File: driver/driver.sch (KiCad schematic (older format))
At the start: 103 parts, among them J1 OUT_A, J10 FAN, J2 OUT_B, J4 RJ45_LED_Shielded, J5 RJ45_LED_Shielded, J6 1602 I2C LCD, J7 IN_VCC, J8 IN_GND, J9 SWD, Q1 TPHR6503PL, Q2 TPHR6503PL, Q3 TPHR6503PL, Q4 TPHR6503PL, U1 MT3608, U10 PC817, U11 AMS1117-5.0, U12 PC817, U13 MAX485E, U2 74HC595, U3 AMS1117-3.3, U4 TC4427, U5 TC4427, U6 STM32F030F4Px, U7 INA226, U8 MCP9804_MSOP, U9 PC817, Y1 8MHz

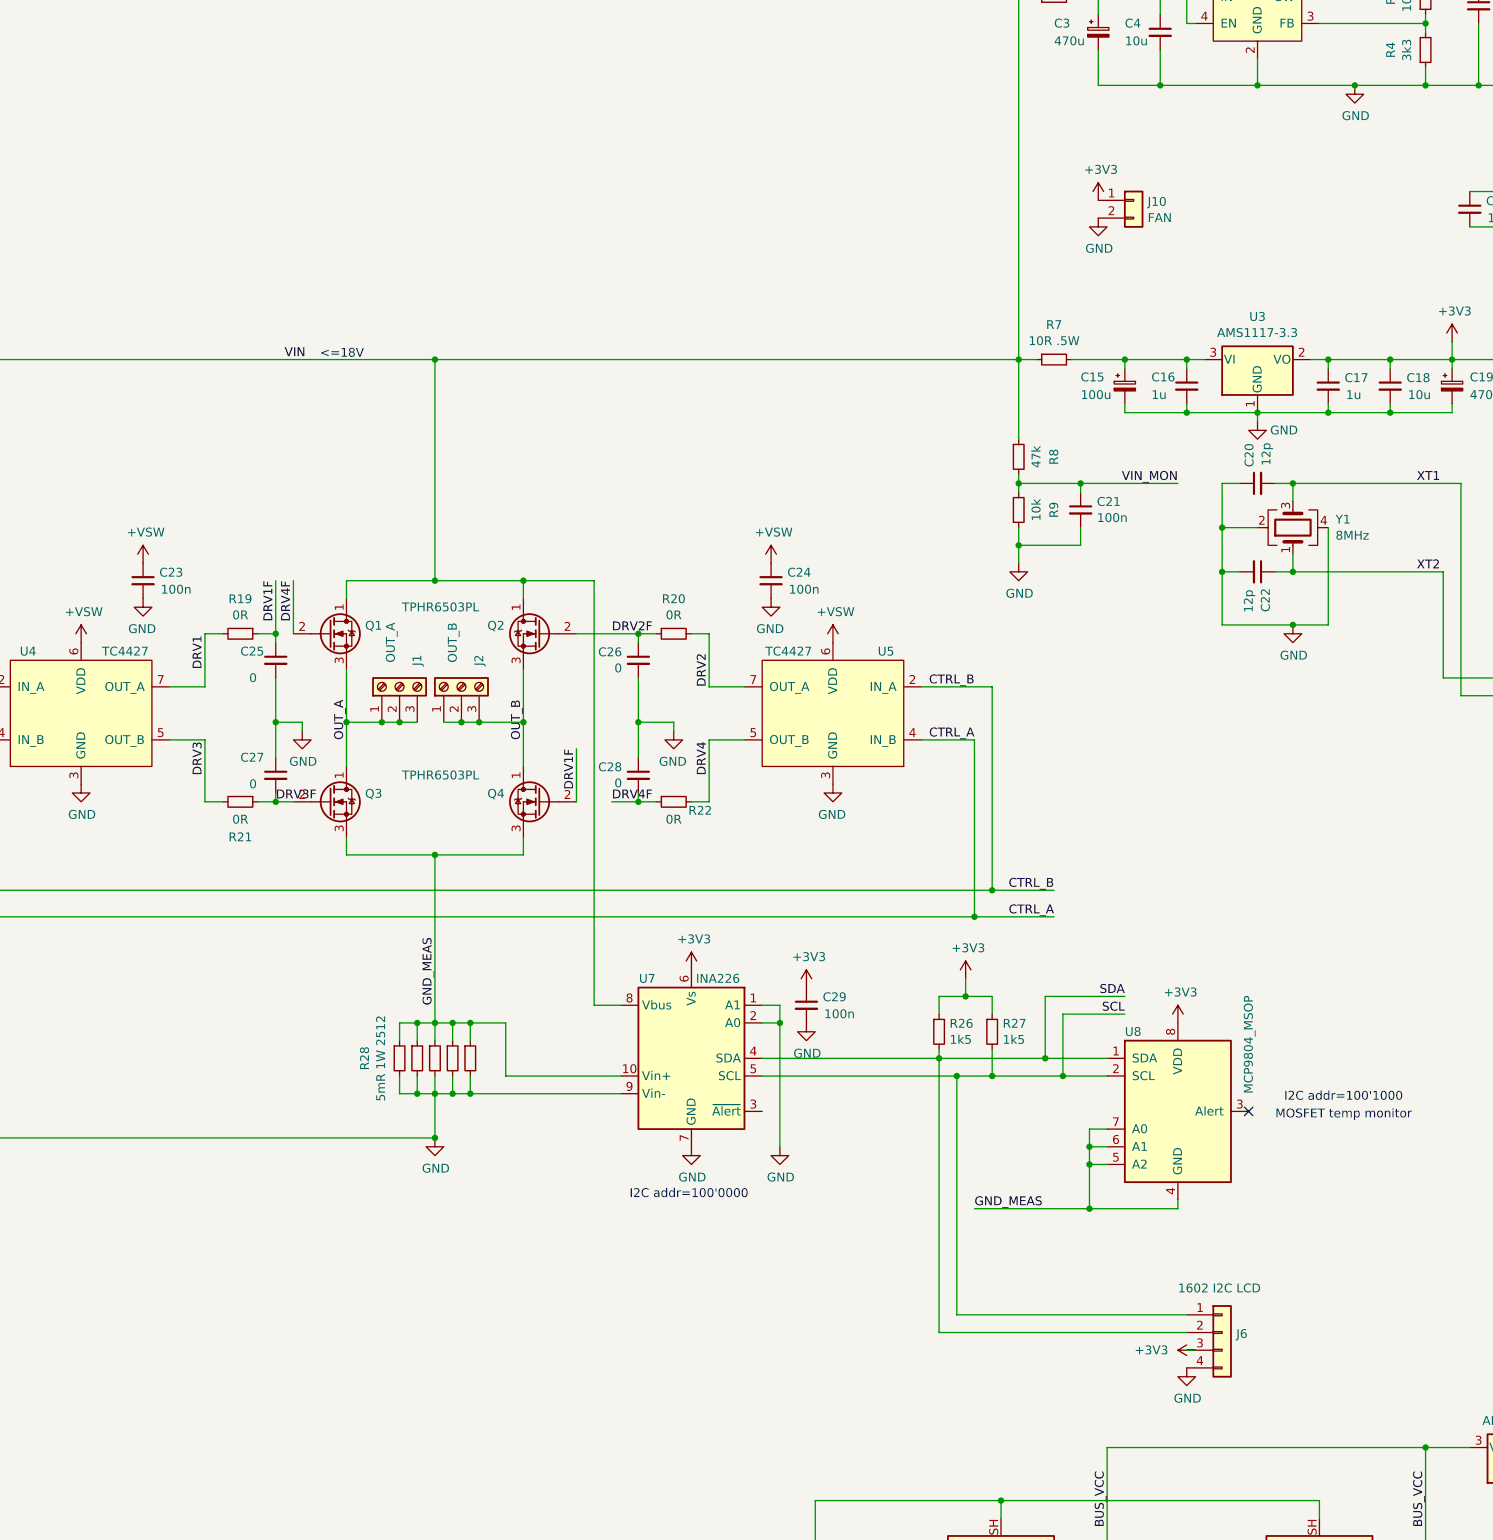
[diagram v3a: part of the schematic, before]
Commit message: driver/fw: Beginnings of a firmware
This code starts up and blinks a led. This means RCC, GPIO and SPI1 are working.
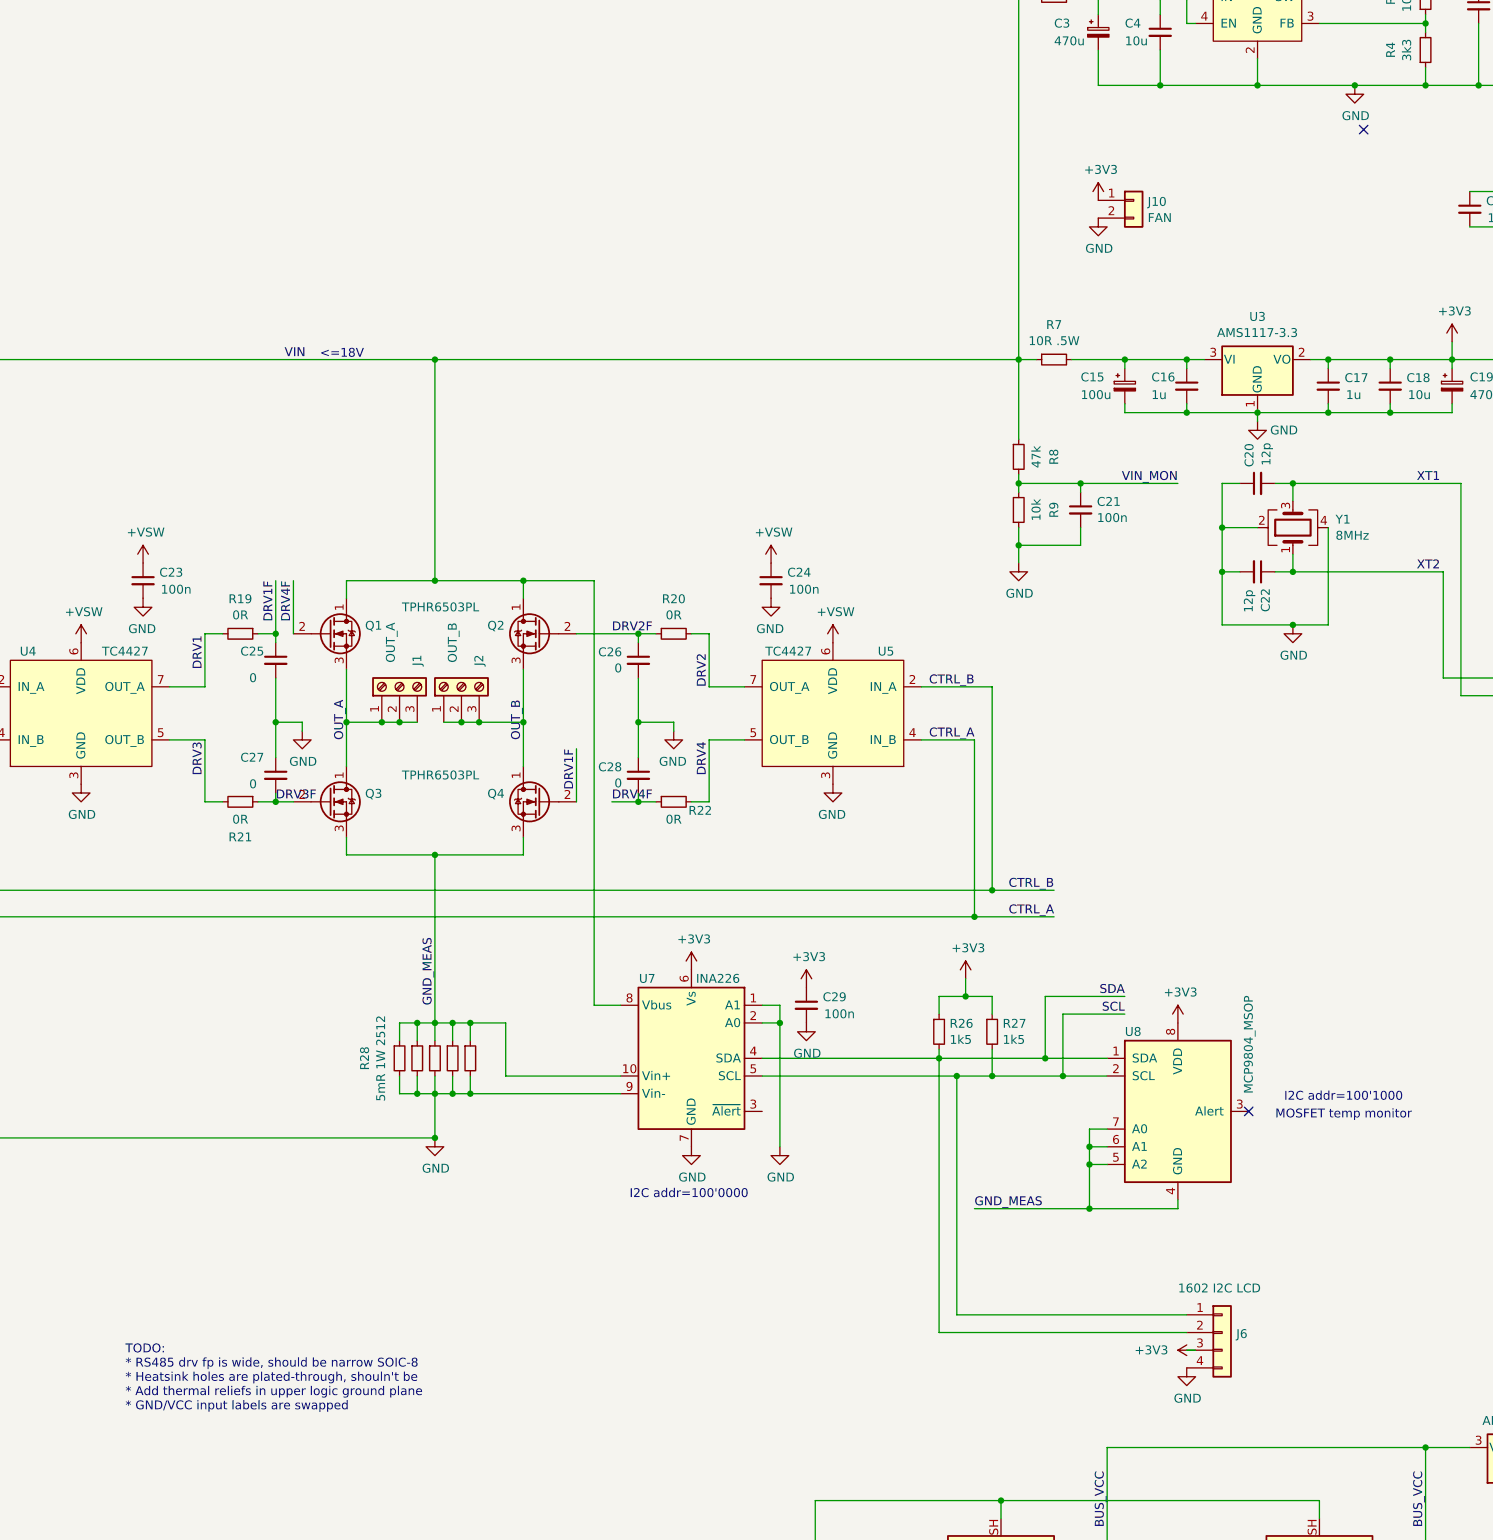
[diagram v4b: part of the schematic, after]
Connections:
- no-connect marks 2 -> 3
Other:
- note added: "TODO:\n* RS485 drv fp is wide, should be narrow SOIC-8\n* Heatsink holes are plated-through, shouln't be\n* Add thermal reliefs in upper logic ground plane\n* GND/VCC input labels are swapped"
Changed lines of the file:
@@
 	1    0    0    -1
 $EndComp
+Text Notes 7600 10050 0    50   ~ 0
+TODO:\n* RS485 drv fp is wide, should be narrow SOIC-8\n* Heatsink holes are plated-through, shouln't be\n* Add thermal reliefs in upper logic ground plane\n* GND/VCC input labels are swapped
+NoConn ~ 14600 2800
 $EndSCHEMATC

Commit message: driver/hw: add a bunch of todos
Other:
- note added: "TODO:\n* RS485 drv fp is wide, should be narrow SOIC-8\n* Heatsink holes are plated-through, shouln't be\n* Add thermal reliefs in upper logic ground plane\n* GND/VCC input labels are swapped\n* White label field for MAC\n* Remove optoisolators\n* Add series resistor to RS485 GND\n* Add decoupling cap next to mosfet temp sensor"
- note removed: "TODO:\n* RS485 drv fp is wide, should be narrow SOIC-8\n* Heatsink holes are plated-through, shouln't be\n* Add thermal reliefs in upper logic ground plane\n* GND/VCC input labels are swapped"
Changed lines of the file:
@@
 EESchema Schematic File Version 4
 LIBS:driver-cache
-EELAYER 26 0
+EELAYER 29 0
 EELAYER END
 $Descr A2 23386 16535
@@
 $EndComp
 Text Notes 7600 10050 0    50   ~ 0
-TODO:\n* RS485 drv fp is wide, should be narrow SOIC-8\n* Heatsink holes are plated-through, shouln't be\n* Add thermal reliefs in upper logic ground plane\n* GND/VCC input labels are swapped
+TODO:\n* RS485 drv fp is wide, should be narrow SOIC-8\n* Heatsink holes are plated-through, shouln't be\n* Add thermal reliefs in upper logic ground plane\n* GND/VCC input labels are swapped\n* White label field for MAC\n* Remove optoisolators\n* Add series resistor to RS485 GND\n* Add decoupling cap next to mosfet temp sensor
 NoConn ~ 14600 2800
 $EndSCHEMATC
